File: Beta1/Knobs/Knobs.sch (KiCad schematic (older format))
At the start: 27 parts, among them U1000 MCP3008T-I/SL, U2 MCP3008T-I/SL

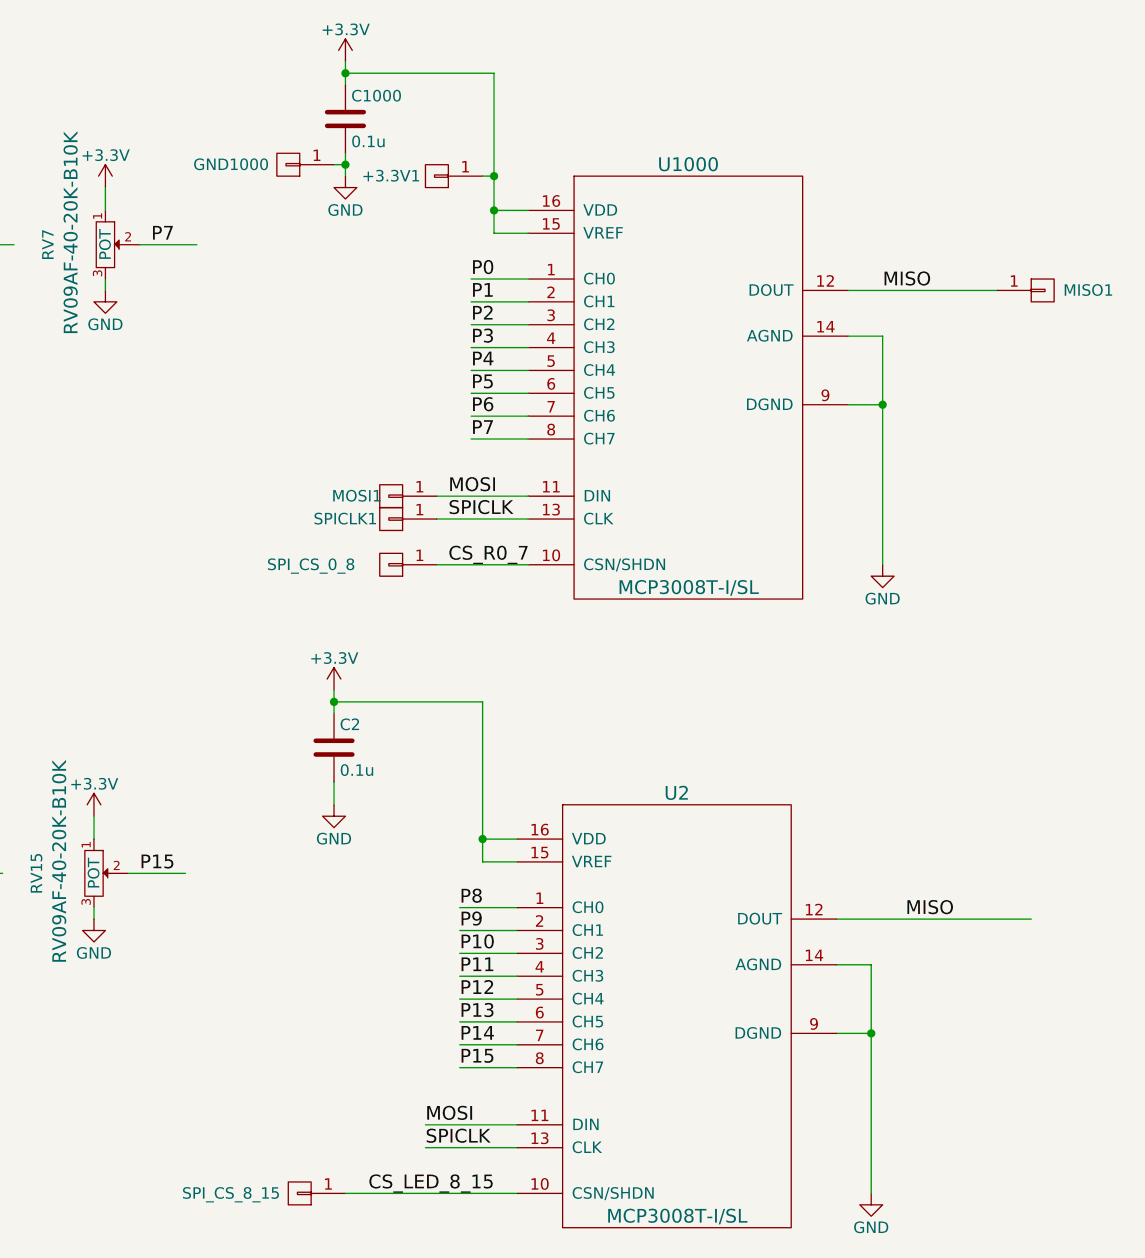
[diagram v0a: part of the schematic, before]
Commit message: Changed second row daisy chain from vias to plated TH. You know. For kids.
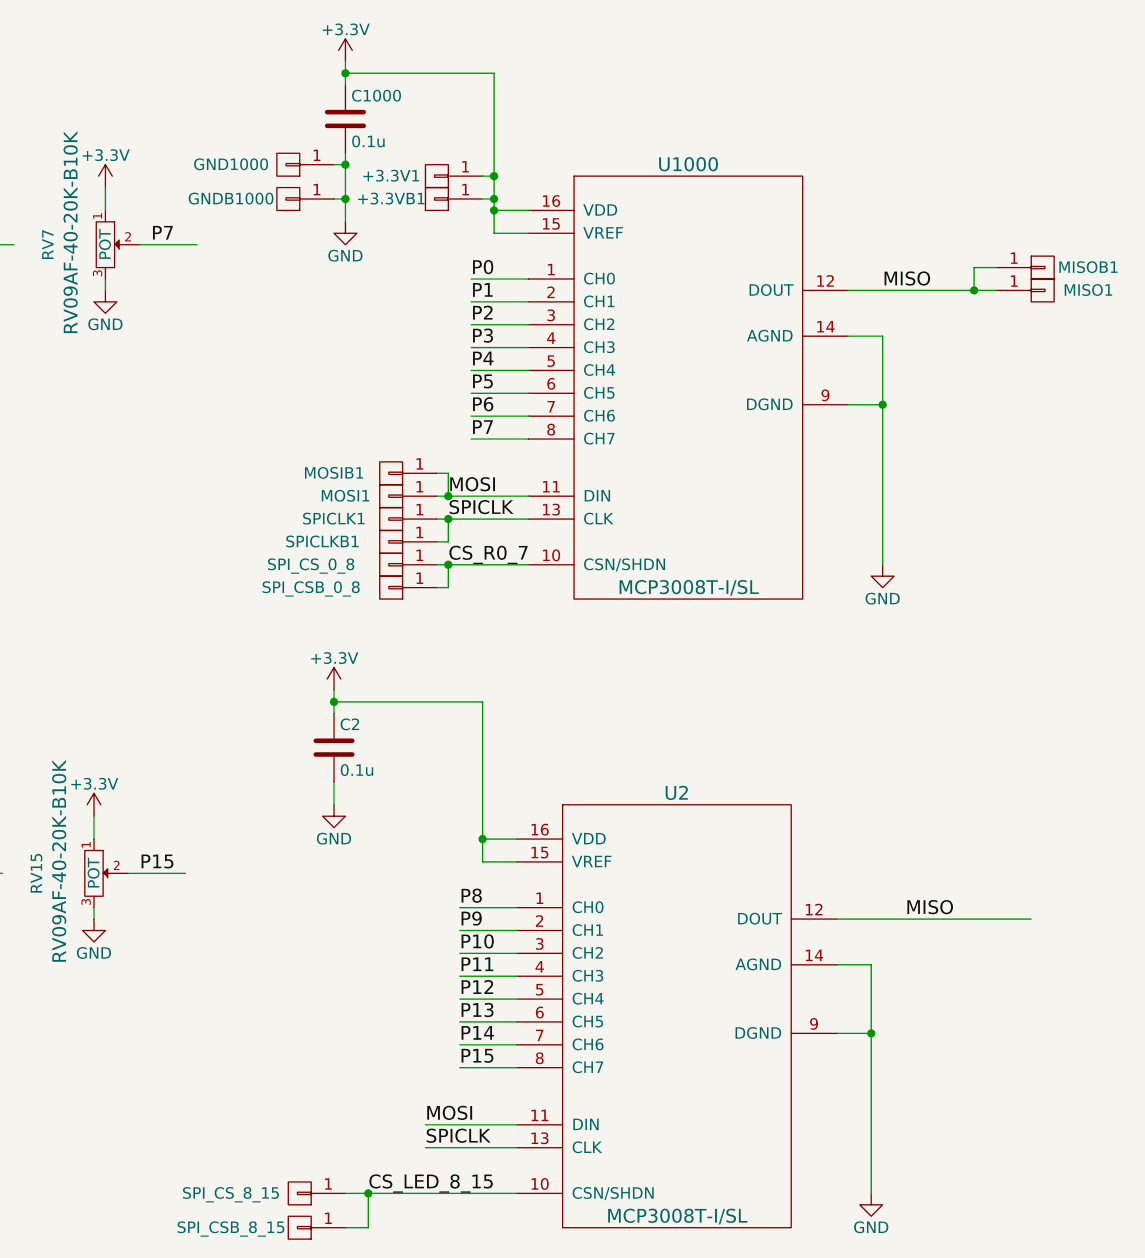
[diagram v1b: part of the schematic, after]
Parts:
- added +3.3VB1, GNDB1000, MISOB1, MOSIB1, SPICLKB1, SPI_CSB_0_8, SPI_CSB_8_15: CONN_01X01, Liberry:single_0.1, symbol CONN_01X01
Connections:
- wire segments 92 -> 104
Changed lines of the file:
@@
 LIBS:Zilog
 LIBS:believotron_wanderlust
-LIBS:KnobLED-cache
 EELAYER 25 0
 EELAYER END
 $Descr B 17000 11000
 encoding utf-8
-Sheet 2 2
+Sheet 1 1
 Title ""
 Date ""
@@
 L GND #PWR017
 U 1 1 582E3FD0
-P 9000 1250
-F 0 "#PWR017" H 9000 1000 50  0001 C CNN
-F 1 "GND" H 9000 1100 50  0000 C CNN
-F 2 "" H 9000 1250 50  0000 C CNN
-F 3 "" H 9000 1250 50  0000 C CNN
-	1    9000 1250
+P 9000 1450
+F 0 "#PWR017" H 9000 1200 50  0001 C CNN
+F 1 "GND" H 9000 1300 50  0000 C CNN
+F 2 "" H 9000 1450 50  0000 C CNN
+F 3 "" H 9000 1450 50  0000 C CNN
+	1    9000 1450
 	1    0    0    -1
 $EndComp
@@
 U 1 1 582E505A
 P 9200 2650
-F 0 "MOSI1" H 9350 2650 50  0000 C CNN
+F 0 "MOSI1" H 9400 2650 50  0000 C CNN
 F 1 "CONN_01X01" V 9300 2650 50  0001 C CNN
 F 2 "Liberry:single_0.1" H 9200 2650 50  0001 C CNN
@@
 U 1 1 582E523F
 P 9200 2750
-F 0 "SPICLK1" H 9400 2750 50  0000 C CNN
+F 0 "SPICLK1" H 9450 2750 50  0000 C CNN
 F 1 "CONN_01X01" V 9300 2750 50  0001 C CNN
 F 2 "Liberry:single_0.1" H 9200 2750 50  0001 C CNN
@@
 	8100 1550 8350 1550
 Wire Wire Line
-	9000 1150 9000 1250
+	9000 1150 9000 1450
 Wire Wire Line
 	9000 750  9000 850
@@
 Text Label 11450 4500 0    60   ~ 0
 MISO
+$Comp
+L CONN_01X01 GNDB1000
+U 1 1 5832E879
+P 8750 1350
+F 0 "GNDB1000" H 9000 1350 50  0000 C CNN
+F 1 "CONN_01X01" V 8850 1350 50  0001 C CNN
+F 2 "Liberry:single_0.1" H 8750 1350 50  0001 C CNN
+F 3 "" H 8750 1350 50  0000 C CNN
+F 4 "PCB" H 8750 1350 60  0001 C CNN "MFG"
+F 5 "ON_PCB" H 8750 1350 60  0001 C CNN "MPN"
+	1    8750 1350
+	-1   0    0    1
+$EndComp
+$Comp
+L CONN_01X01 +3.3VB1
+U 1 1 5832E8E1
+P 9400 1350
+F 0 "+3.3VB1" H 9600 1350 50  0000 C CNN
+F 1 "CONN_01X01" V 9500 1350 50  0001 C CNN
+F 2 "Liberry:single_0.1" H 9400 1350 50  0001 C CNN
+F 3 "" H 9400 1350 50  0000 C CNN
+F 4 "PCB" H 9400 1350 60  0001 C CNN "MFG"
+F 5 "ON_PCB" H 9400 1350 60  0001 C CNN "MPN"
+	1    9400 1350
+	-1   0    0    1
+$EndComp
+$Comp
+L CONN_01X01 MOSIB1
+U 1 1 5832EC50
+P 9200 2550
+F 0 "MOSIB1" H 9450 2550 50  0000 C CNN
+F 1 "CONN_01X01" V 9300 2550 50  0001 C CNN
+F 2 "Liberry:single_0.1" H 9200 2550 50  0001 C CNN
+F 3 "" H 9200 2550 50  0000 C CNN
+F 4 "PCB" H 9200 2550 60  0001 C CNN "MFG"
+F 5 "ON_PCB" H 9200 2550 60  0001 C CNN "MPN"
+	1    9200 2550
+	-1   0    0    1
+$EndComp
+$Comp
+L CONN_01X01 SPICLKB1
+U 1 1 5832ECC2
+P 9200 2850
+F 0 "SPICLKB1" H 9500 2850 50  0000 C CNN
+F 1 "CONN_01X01" V 9300 2850 50  0001 C CNN
+F 2 "Liberry:single_0.1" H 9200 2850 50  0001 C CNN
+F 3 "" H 9200 2850 50  0000 C CNN
+F 4 "PCB" H 9200 2850 60  0001 C CNN "MFG"
+F 5 "ON_PCB" H 9200 2850 60  0001 C CNN "MPN"
+	1    9200 2850
+	-1   0    0    1
+$EndComp
+$Comp
+L CONN_01X01 SPI_CSB_0_8
+U 1 1 5832ED37
+P 9200 3050
+F 0 "SPI_CSB_0_8" H 9550 3050 50  0000 C CNN
+F 1 "CONN_01X01" V 9300 3050 50  0001 C CNN
+F 2 "Liberry:single_0.1" H 9200 3050 50  0001 C CNN
+F 3 "" H 9200 3050 50  0000 C CNN
+F 4 "PCB" H 9200 3050 60  0001 C CNN "MFG"
+F 5 "ON_PCB" H 9200 3050 60  0001 C CNN "MPN"
+	1    9200 3050
+	-1   0    0    1
+$EndComp
+$Comp
+L CONN_01X01 MISOB1
+U 1 1 5832F20B
+P 12050 1650
+F 0 "MISOB1" H 12250 1650 50  0000 C CNN
+F 1 "CONN_01X01" V 12150 1650 50  0001 C CNN
+F 2 "Liberry:single_0.1" H 12050 1650 50  0001 C CNN
+F 3 "" H 12050 1650 50  0000 C CNN
+F 4 "PCB" H 12050 1650 60  0001 C CNN "MFG"
+F 5 "ON_PCB" H 12050 1650 60  0001 C CNN "MPN"
+	1    12050 1650
+	1    0    0    -1
+$EndComp
+Wire Wire Line
+	11850 1650 11750 1650
+Wire Wire Line
+	11750 1650 11750 1750
+Connection ~ 11750 1750
+Wire Wire Line
+	9400 2550 9450 2550
+Wire Wire Line
+	9450 2550 9450 2650
+Connection ~ 9450 2650
+Wire Wire Line
+	9400 2850 9450 2850
+Wire Wire Line
+	9450 2850 9450 2750
+Connection ~ 9450 2750
+Wire Wire Line
+	9400 3050 9450 3050
+Wire Wire Line
+	9450 3050 9450 2950
+Connection ~ 9450 2950
+Wire Wire Line
+	9600 1350 9650 1350
+Connection ~ 9650 1350
+Wire Wire Line
+	8950 1350 9000 1350
+Connection ~ 9000 1350
+$Comp
+L CONN_01X01 SPI_CSB_8_15
+U 1 1 583313D9
+P 8800 5850
+F 0 "SPI_CSB_8_15" H 9100 5850 50  0000 C CNN
+F 1 "CONN_01X01" V 8900 5850 50  0001 C CNN
+F 2 "Liberry:single_0.1" H 8800 5850 50  0001 C CNN
+F 3 "" H 8800 5850 50  0000 C CNN
+F 4 "PCB" H 8800 5850 60  0001 C CNN "MFG"
+F 5 "ON_PCB" H 8800 5850 60  0001 C CNN "MPN"
+	1    8800 5850
+	-1   0    0    1
+$EndComp
+Wire Wire Line
+	9000 5850 9100 5850
+Wire Wire Line
+	9100 5850 9100 5700
+Connection ~ 9100 5700
 $EndSCHEMATC

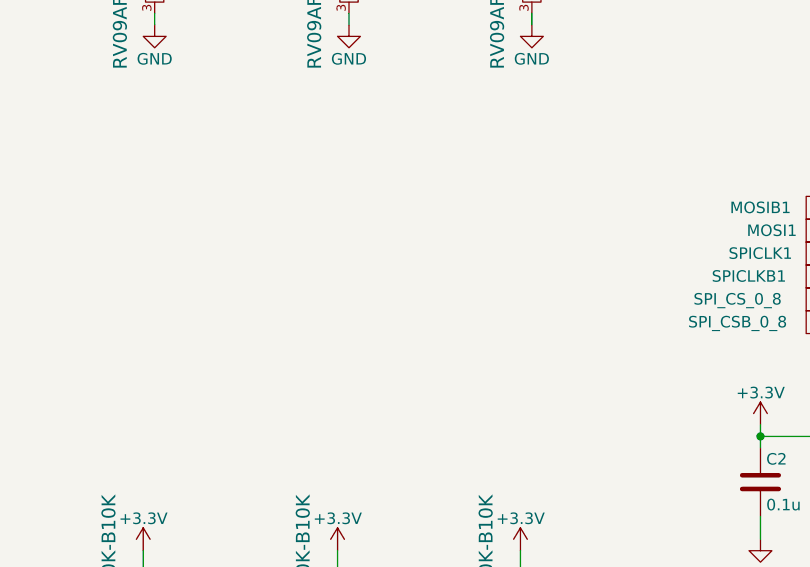
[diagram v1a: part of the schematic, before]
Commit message: Catchup Commit.  Non-atomic, Refactored LED, Keyboard, KeyPAD, and Knobs PCBs
LED: Changed chips. Cleaned up silkscreen text. Added some support
mounting holes. Shrank height of board to avoid stackup. KeyPAD is
updated with new footprint. Keyboard and Knobs are unknown.
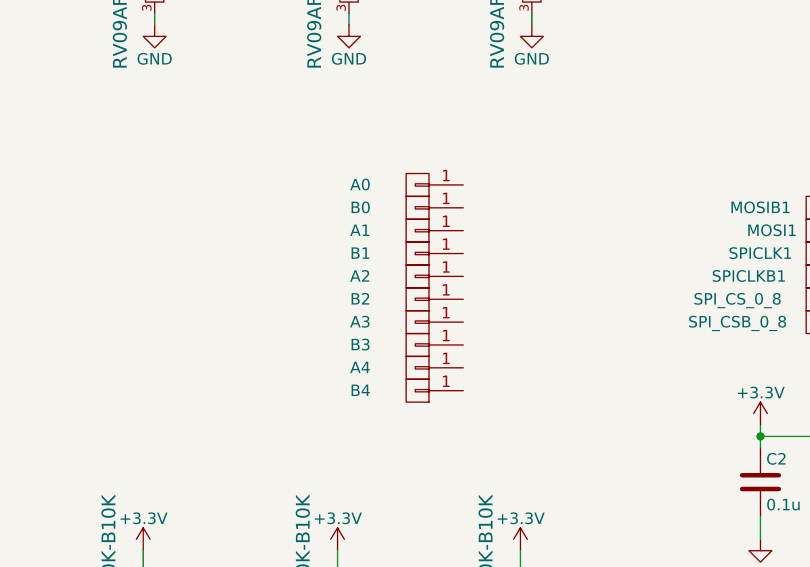
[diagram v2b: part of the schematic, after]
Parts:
- added A0, A1, A2, A3, A4, B0, B1, B2, B3, B4: CONN_01X01, Liberry:single_0.1, symbol CONN_01X01
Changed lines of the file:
@@
 LIBS:Zilog
 LIBS:believotron_wanderlust
+LIBS:Knobs-cache
 EELAYER 25 0
 EELAYER END
@@
 	9100 5850 9100 5700
 Connection ~ 9100 5700
+$Comp
+L CONN_01X01 A0
+U 1 1 58336F43
+P 7450 2450
+F 0 "A0" H 7700 2450 50  0000 C CNN
+F 1 "CONN_01X01" V 7550 2450 50  0001 C CNN
+F 2 "Liberry:single_0.1" H 7450 2450 50  0001 C CNN
+F 3 "" H 7450 2450 50  0000 C CNN
+F 4 "PCB" H 7450 2450 60  0001 C CNN "MFG"
+F 5 "ON_PCB" H 7450 2450 60  0001 C CNN "MPN"
+	1    7450 2450
+	-1   0    0    1
+$EndComp
+$Comp
+L CONN_01X01 B0
+U 1 1 583370FC
+P 7450 2550
+F 0 "B0" H 7700 2550 50  0000 C CNN
+F 1 "CONN_01X01" V 7550 2550 50  0001 C CNN
+F 2 "Liberry:single_0.1" H 7450 2550 50  0001 C CNN
+F 3 "" H 7450 2550 50  0000 C CNN
+F 4 "PCB" H 7450 2550 60  0001 C CNN "MFG"
+F 5 "ON_PCB" H 7450 2550 60  0001 C CNN "MPN"
+	1    7450 2550
+	-1   0    0    1
+$EndComp
+$Comp
+L CONN_01X01 A1
+U 1 1 5833717C
+P 7450 2650
+F 0 "A1" H 7700 2650 50  0000 C CNN
+F 1 "CONN_01X01" V 7550 2650 50  0001 C CNN
+F 2 "Liberry:single_0.1" H 7450 2650 50  0001 C CNN
+F 3 "" H 7450 2650 50  0000 C CNN
+F 4 "PCB" H 7450 2650 60  0001 C CNN "MFG"
+F 5 "ON_PCB" H 7450 2650 60  0001 C CNN "MPN"
+	1    7450 2650
+	-1   0    0    1
+$EndComp
+$Comp
+L CONN_01X01 B1
+U 1 1 58337207
+P 7450 2750
+F 0 "B1" H 7700 2750 50  0000 C CNN
+F 1 "CONN_01X01" V 7550 2750 50  0001 C CNN
+F 2 "Liberry:single_0.1" H 7450 2750 50  0001 C CNN
+F 3 "" H 7450 2750 50  0000 C CNN
+F 4 "PCB" H 7450 2750 60  0001 C CNN "MFG"
+F 5 "ON_PCB" H 7450 2750 60  0001 C CNN "MPN"
+	1    7450 2750
+	-1   0    0    1
+$EndComp
+$Comp
+L CONN_01X01 A2
+U 1 1 58337609
+P 7450 2850
+F 0 "A2" H 7700 2850 50  0000 C CNN
+F 1 "CONN_01X01" V 7550 2850 50  0001 C CNN
+F 2 "Liberry:single_0.1" H 7450 2850 50  0001 C CNN
+F 3 "" H 7450 2850 50  0000 C CNN
+F 4 "PCB" H 7450 2850 60  0001 C CNN "MFG"
+F 5 "ON_PCB" H 7450 2850 60  0001 C CNN "MPN"
+	1    7450 2850
+	-1   0    0    1
+$EndComp
+$Comp
+L CONN_01X01 B2
+U 1 1 58337611
+P 7450 2950
+F 0 "B2" H 7700 2950 50  0000 C CNN
+F 1 "CONN_01X01" V 7550 2950 50  0001 C CNN
+F 2 "Liberry:single_0.1" H 7450 2950 50  0001 C CNN
+F 3 "" H 7450 2950 50  0000 C CNN
+F 4 "PCB" H 7450 2950 60  0001 C CNN "MFG"
+F 5 "ON_PCB" H 7450 2950 60  0001 C CNN "MPN"
+	1    7450 2950
+	-1   0    0    1
+$EndComp
+$Comp
+L CONN_01X01 A3
+U 1 1 58337619
+P 7450 3050
+F 0 "A3" H 7700 3050 50  0000 C CNN
+F 1 "CONN_01X01" V 7550 3050 50  0001 C CNN
+F 2 "Liberry:single_0.1" H 7450 3050 50  0001 C CNN
+F 3 "" H 7450 3050 50  0000 C CNN
+F 4 "PCB" H 7450 3050 60  0001 C CNN "MFG"
+F 5 "ON_PCB" H 7450 3050 60  0001 C CNN "MPN"
+	1    7450 3050
+	-1   0    0    1
+$EndComp
+$Comp
+L CONN_01X01 B3
+U 1 1 58337621
+P 7450 3150
+F 0 "B3" H 7700 3150 50  0000 C CNN
+F 1 "CONN_01X01" V 7550 3150 50  0001 C CNN
+F 2 "Liberry:single_0.1" H 7450 3150 50  0001 C CNN
+F 3 "" H 7450 3150 50  0000 C CNN
+F 4 "PCB" H 7450 3150 60  0001 C CNN "MFG"
+F 5 "ON_PCB" H 7450 3150 60  0001 C CNN "MPN"
+	1    7450 3150
+	-1   0    0    1
+$EndComp
+$Comp
+L CONN_01X01 A4
+U 1 1 58337C21
+P 7450 3250
+F 0 "A4" H 7700 3250 50  0000 C CNN
+F 1 "CONN_01X01" V 7550 3250 50  0001 C CNN
+F 2 "Liberry:single_0.1" H 7450 3250 50  0001 C CNN
+F 3 "" H 7450 3250 50  0000 C CNN
+F 4 "PCB" H 7450 3250 60  0001 C CNN "MFG"
+F 5 "ON_PCB" H 7450 3250 60  0001 C CNN "MPN"
+	1    7450 3250
+	-1   0    0    1
+$EndComp
+$Comp
+L CONN_01X01 B4
+U 1 1 58337C29
+P 7450 3350
+F 0 "B4" H 7700 3350 50  0000 C CNN
+F 1 "CONN_01X01" V 7550 3350 50  0001 C CNN
+F 2 "Liberry:single_0.1" H 7450 3350 50  0001 C CNN
+F 3 "" H 7450 3350 50  0000 C CNN
+F 4 "PCB" H 7450 3350 60  0001 C CNN "MFG"
+F 5 "ON_PCB" H 7450 3350 60  0001 C CNN "MPN"
+	1    7450 3350
+	-1   0    0    1
+$EndComp
 $EndSCHEMATC
